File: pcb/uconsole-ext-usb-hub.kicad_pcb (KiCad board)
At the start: 2 copper layers, 32.1 x 77 mm, 38 parts, among them J1 MINI_PCIE, J2 SPEAKER, J3 SPEAKER, P1 USB_C_Plug_USB2.0, P2 USB_C_Plug_USB2.0, P3 USB_C_Plug_USB2.0, P4 USB_C_Plug_USB2.0, U1 TUSB2048B, U2 TPS2044D, U3 USBLC6-2P6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

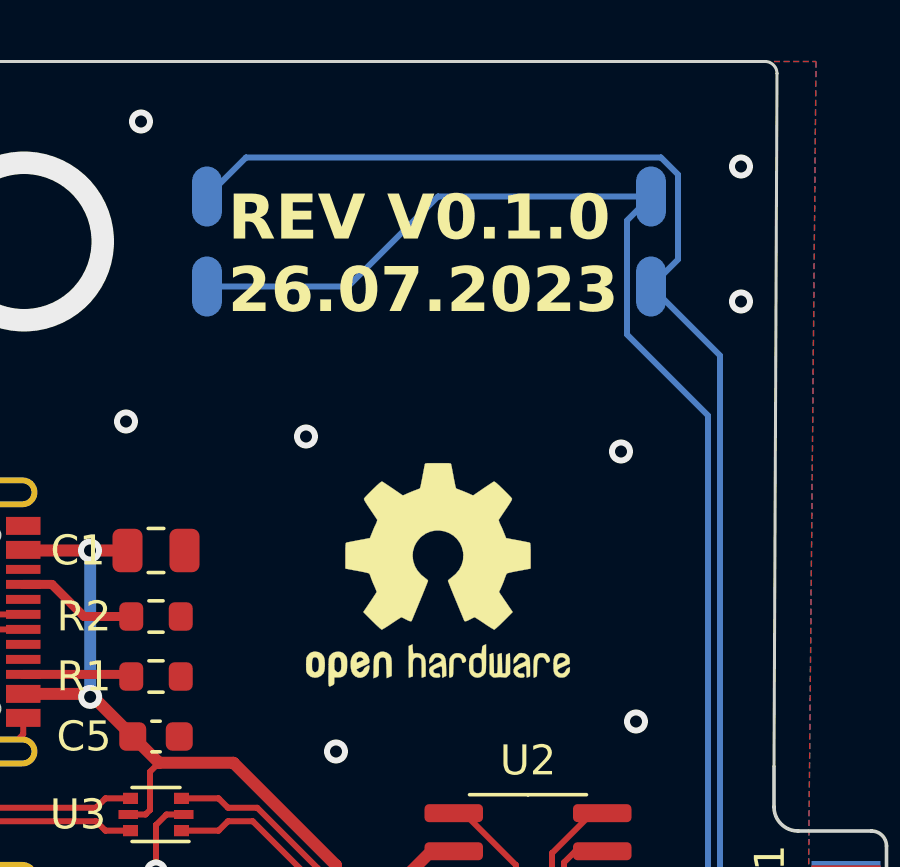
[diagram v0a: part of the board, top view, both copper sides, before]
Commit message: Update version to 0.1.1
* Add OSHWA certification mark
* Add license info
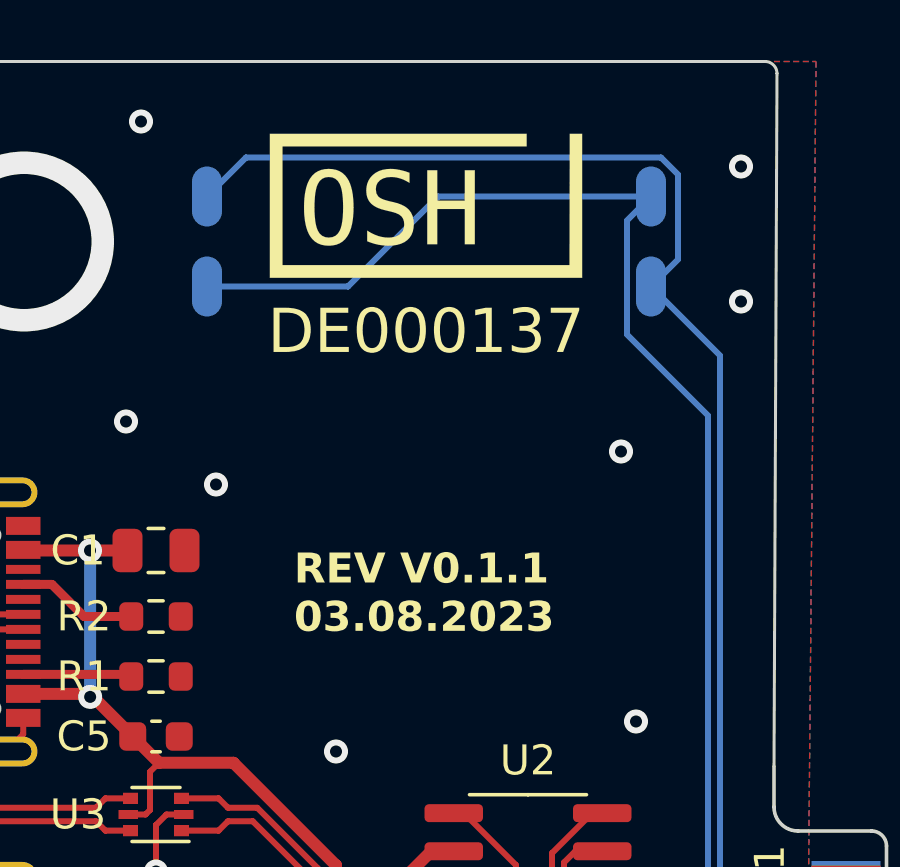
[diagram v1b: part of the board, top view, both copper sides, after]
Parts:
- removed the REF** at (156.4, 78.6)
- added OSHW_Dual_0.25_Scale: DE000137, oshwa-marks:OSHW_Dual_0.25_Scale, F.Cu at (156.0, 66.0)
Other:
- board text added: "REV V0.1.1 03.08.2023"
- board text removed: "REV V0.1.0 26.07.2023"
